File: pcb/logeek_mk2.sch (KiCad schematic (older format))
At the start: 131 parts, among them P1 Power, P10 XH2.54-2P RA, P11 BARREL_JACK, P12 USB_B, P13 DC3 5x2, P14 Power, P15 Analog, P16 Digital, P17 Digital, P2 Analog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

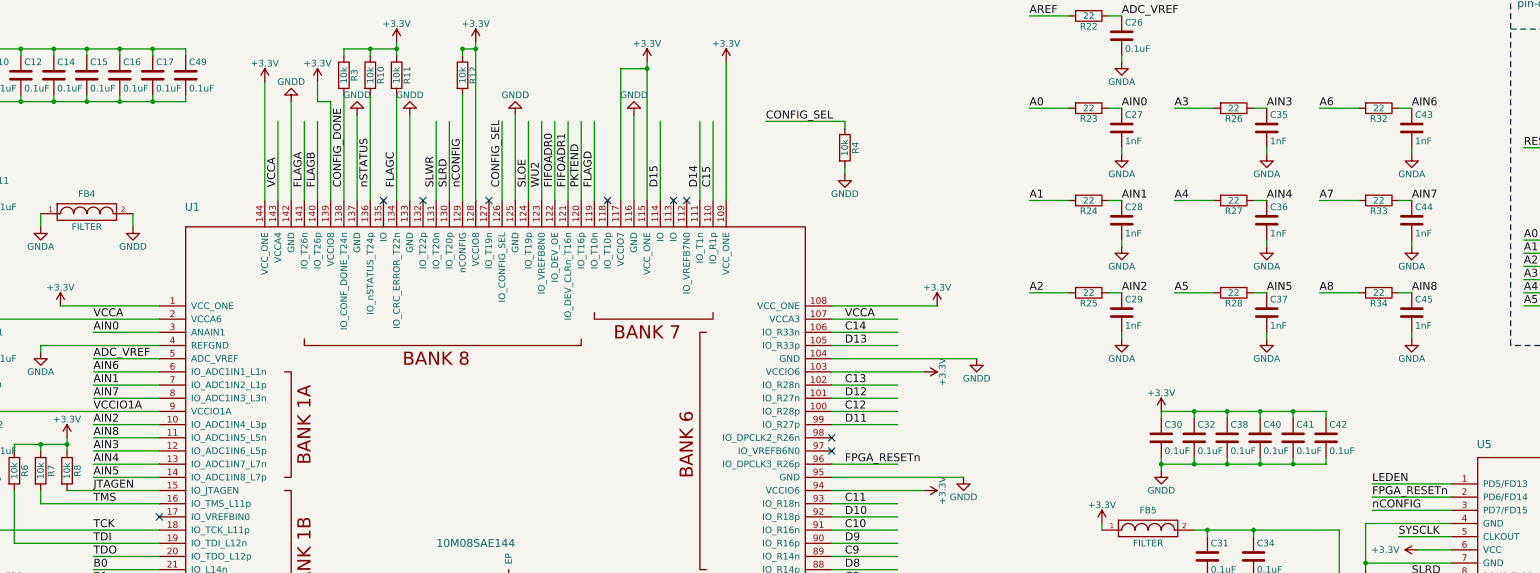
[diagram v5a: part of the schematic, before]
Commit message: Analog pin-mapping changed to support VIN monitoring.
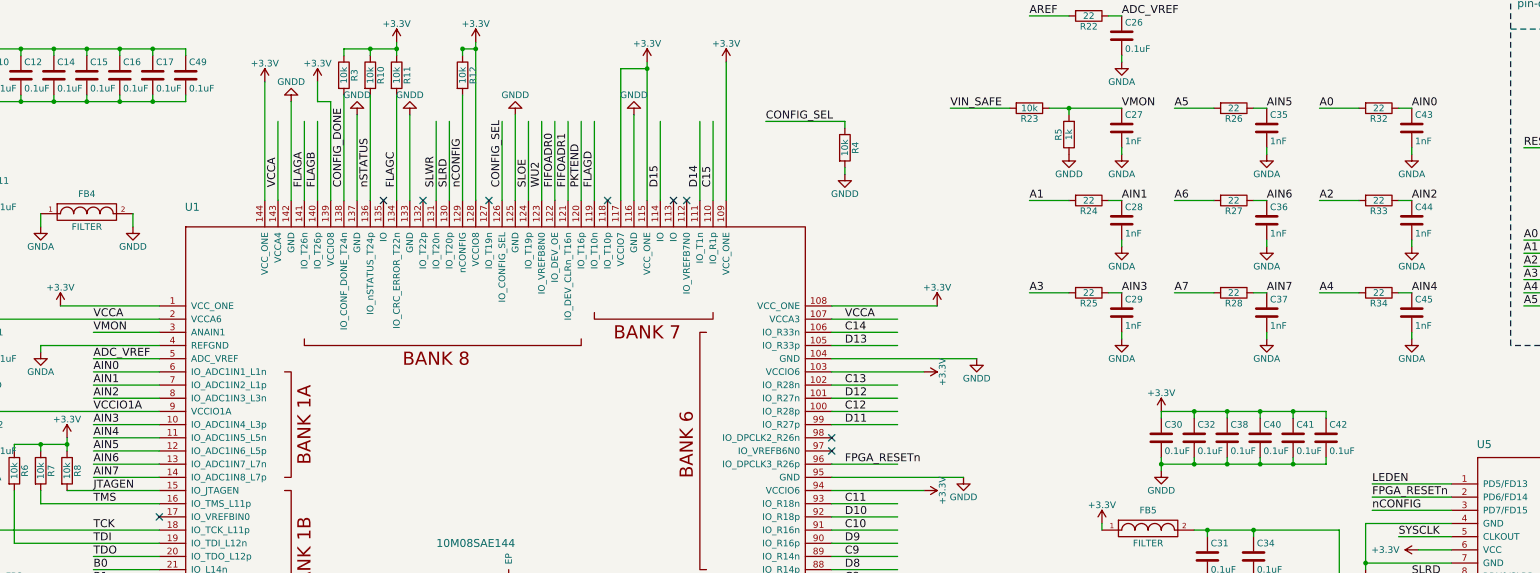
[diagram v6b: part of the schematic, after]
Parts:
- added R5: 1k, Logeek_MK2:R_0402_HandSoldering, symbol R
- R23: value 22 -> 10k
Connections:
- net labels added: VMON
- net labels removed: AIN8
- wire segments 542 -> 543
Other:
- moved on the sheet: R23
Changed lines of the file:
@@
 ADC_VREF
 Text Label 2600 3150 0    60   ~ 0
-AIN0
+VMON
 Text Label 2600 3550 0    60   ~ 0
 AIN1
 Text Label 2600 3850 0    60   ~ 0
-AIN2
-Text Label 2600 4050 0    60   ~ 0
 AIN3
+Text Label 2600 4050 0    60   ~ 0
+AIN5
 Text Label 2600 4150 0    60   ~ 0
-AIN4
+AIN6
 Text Label 2600 4250 0    60   ~ 0
-AIN5
+AIN7
 $Comp
 L GNDA #PWR04
@@
 L R R23
 U 1 1 55AFC66C
-P 10150 1450
-F 0 "R23" V 10230 1450 50  0000 C CNN
-F 1 "22" V 10150 1450 50  0000 C CNN
-F 2 "Resistors_SMD:R_0402_HandSoldering" V 10080 1450 30  0001 C CNN
-F 3 "" H 10150 1450 30  0000 C CNN
-	1    10150 1450
+P 9700 1450
+F 0 "R23" V 9780 1450 50  0000 C CNN
+F 1 "10k" V 9700 1450 50  0000 C CNN
+F 2 "Resistors_SMD:R_0402_HandSoldering" V 9630 1450 30  0001 C CNN
+F 3 "" H 9700 1450 30  0000 C CNN
+	1    9700 1450
 	0    1    1    0
 $EndComp
-Text Label 9700 1450 0    60   ~ 0
-A0
+Text Label 9100 1450 0    60   ~ 0
+VIN_SAFE
 Text Label 10400 1450 0    60   ~ 0
-AIN0
+VMON
 $Comp
 L R R24
@@
 $EndComp
 Text Label 9700 2850 0    60   ~ 0
-A2
+A3
 Text Label 10400 2850 0    60   ~ 0
-AIN2
+AIN3
 $Comp
 L R R26
@@
 $EndComp
 Text Label 10800 1450 0    60   ~ 0
-A3
+A5
 Text Label 11500 1450 0    60   ~ 0
-AIN3
+AIN5
 $Comp
 L R R27
@@
 $EndComp
 Text Label 10800 2150 0    60   ~ 0
-A4
+A6
 Text Label 11500 2150 0    60   ~ 0
-AIN4
+AIN6
 $Comp
 L R R28
@@
 $EndComp
 Text Label 10800 2850 0    60   ~ 0
-A5
+A7
 Text Label 11500 2850 0    60   ~ 0
-AIN5
+AIN7
 $Comp
 L C C26
@@
 CPU_RESETn
 Text Label 2600 3450 0    60   ~ 0
-AIN6
+AIN0
 Text Label 2600 3650 0    60   ~ 0
-AIN7
+AIN2
 Text Label 2600 3950 0    60   ~ 0
-AIN8
+AIN4
 $Comp
 L R R32
@@
 $EndComp
 Text Label 11900 1450 0    60   ~ 0
-A6
+A0
 Text Label 12600 1450 0    60   ~ 0
-AIN6
+AIN0
 $Comp
 L R R33
@@
 $EndComp
 Text Label 11900 2150 0    60   ~ 0
-A7
+A2
 Text Label 12600 2150 0    60   ~ 0
-AIN7
+AIN2
 $Comp
 L R R34
@@
 $EndComp
 Text Label 11900 2850 0    60   ~ 0
-A8
+A4
 Text Label 12600 2850 0    60   ~ 0
-AIN8
+AIN4
 $Comp
 L C C43
@@
 	9700 2150 10000 2150
 Wire Wire Line
-	10400 1450 10300 1450
+	9850 1450 10400 1450
 Wire Wire Line
-	9700 1450 10000 1450
+	9100 1450 9550 1450
 Wire Wire Line
 	10400 750  10300 750
@@
 EXTCLK
 NoConn ~ 7000 2150
+$Comp
+L R R5
+U 1 1 5667791F
+P 10000 1650
+F 0 "R5" V 10080 1650 50  0000 C CNN
+F 1 "1k" V 10000 1650 50  0000 C CNN
+F 2 "Logeek_MK2:R_0402_HandSoldering" V 9930 1650 30  0001 C CNN
+F 3 "" H 10000 1650 30  0000 C CNN
+	1    10000 1650
+	-1   0    0    1
+$EndComp
+$Comp
+L GNDD #PWR0114
+U 1 1 56677B15
+P 10000 1800
+F 0 "#PWR0114" H 10000 1550 50  0001 C CNN
+F 1 "GNDD" H 10000 1650 50  0000 C CNN
+F 2 "" H 10000 1800 60  0000 C CNN
+F 3 "" H 10000 1800 60  0000 C CNN
+	1    10000 1800
+	1    0    0    -1
+$EndComp
+Wire Wire Line
+	10000 1500 10000 1450
+Connection ~ 10000 1450
 $EndSCHEMATC

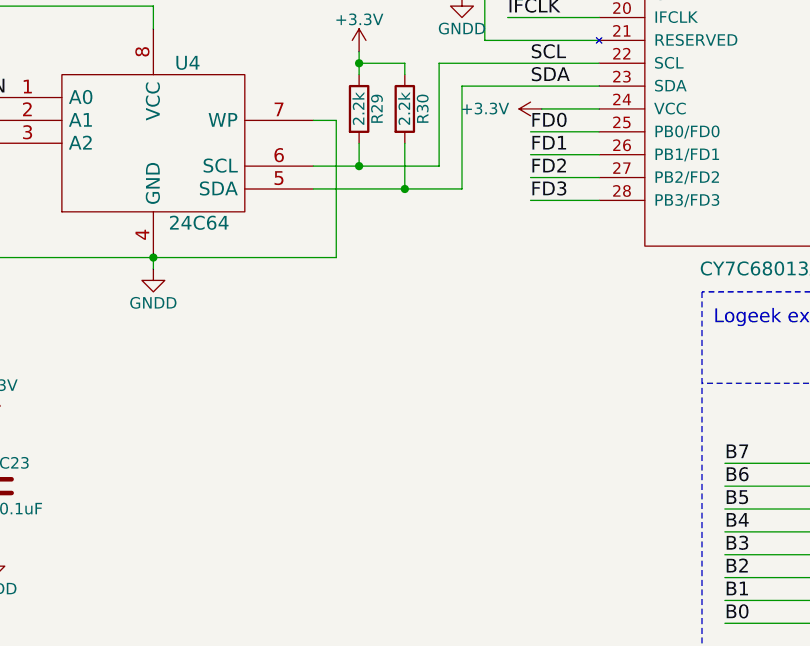
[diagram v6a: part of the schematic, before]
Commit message: FPGA footprint center pad updated.
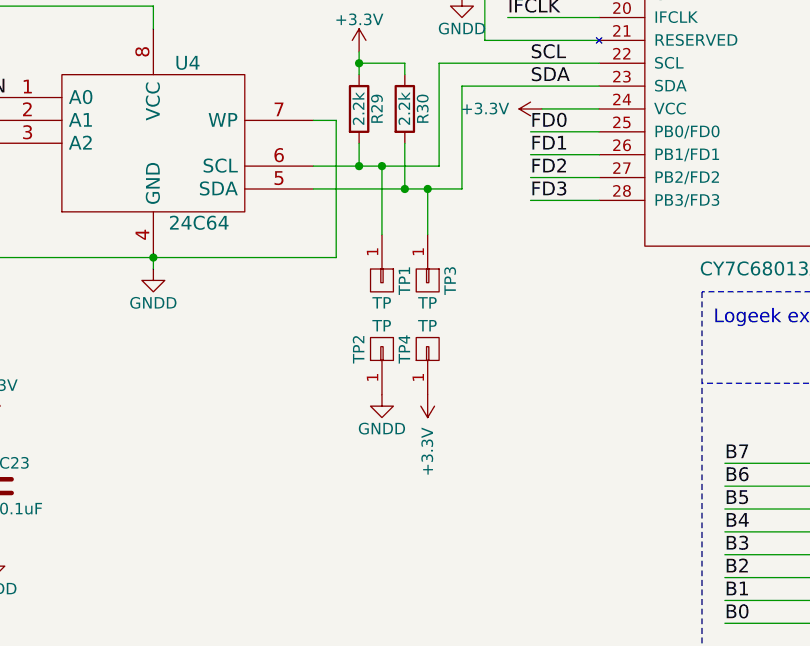
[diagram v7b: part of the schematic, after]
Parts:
- added TP1, TP2, TP3, TP4: TP, Logeek_MK2:Test_Point_1Pin, symbol CONN_01X01
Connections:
- wire segments 543 -> 545

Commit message: Silkscreen art updated.
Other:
- moved on the sheet: C28, C29, C35, C36, C37, C43, C44, C45, R24, R25, R26, R27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
